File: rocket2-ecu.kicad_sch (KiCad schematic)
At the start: 25 parts, among them J1 ALARM, J2 SMA, P1 PAD_SMD, P2 PAD_SMD, P3 PAD_SMD, P4 PAD_SMD, Q1 DMG3402L

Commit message: ECU essentially reviewable
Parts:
- removed C2: 100nF, Capacitor_SMD:C_0603_1608Metric, symbol Device:C_Small
- removed C7: 10uF, Capacitor_SMD:C_0603_1608Metric, symbol Device:C_Small
- removed J2: SMA, Connector_Coaxial:SMA_Molex_73251-2200_Horizontal, symbol Connector:Conn_Coaxial
- removed U3: ~, Package_SO:SOIC-8W_5.3x5.3mm_P1.27mm, symbol UCIRP-KiCAD-Lib:SST25VF016B
- removed U4: ~, UCIRP-KiCAD-Lib:RFM95W, symbol UCIRP-KiCAD-Lib:RFM95W
- renumbered C3 to C2, C4 to C3, C5 to C4, C6 to C5, C8 to C6, U5 to U3, U6 to U4
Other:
- added sheet ECU_Memory (ECU_Memory.kicad_sch)
- added sheet ECU_Radios (ECU_Radios.kicad_sch)
- note added: "ECU Radios"
- note added: "I want this to actually work"
- note removed: "SOMETHING NEEDS TO BE FIXED IN EVE I FORGOT WHAT"
- note removed: "TRS Radio Module"

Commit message: addressed PR comments
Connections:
- no-connect marks 0 -> 1
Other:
- added sheet PT5 (pt.kicad_sch)
- added sheet PT6 (pt.kicad_sch)
- added sheet TC1 (tc.kicad_sch)
- note added: "1 extra TC (NEED TO ADD CS TO STM)"
- note added: "Two extra PTs for redundancy (5 and 6) (NEED TO ADD TO STM)"
- moved on the sheet: P1, P2, P3, P4

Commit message: Updated schematic with IOC
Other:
- note removed: "1 extra TC (NEED TO ADD CS TO STM)"
- note removed: "Two extra PTs for redundancy (5 and 6) (NEED TO ADD TO STM)"
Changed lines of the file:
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@@
-		)
-	)
-	(text "1 extra TC\n\n(NEED TO ADD CS \nTO STM)"
-		(exclude_from_sim no)
-		(at 113.284 174.244 0)
-		(effects
-			(font
-				(size 1.27 1.27)
-				(color 255 26 30 1)
-			)
-		)
-	)
-	(text "Two extra PTs \nfor redundancy \n(5 and 6)\n\n(NEED TO ADD TO STM)"
-		(exclude_from_sim no)
-		(at 69.85 148.844 0)
-		(effects
-			(font
-				(size 1.27 1.27)
-				(color 255 26 30 1)
-			)
 		)
 	)

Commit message: Assigned almost all footprints
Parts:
- C1, C2, C3, C4, C5: footprint Capacitor_SMD:C_0603_1608Metric -> Capacitor_SMD:C_0402_1005Metric; Part # (none) -> Generic 100nF 6.3V X7R 0402 MLCC
- P1, P2, P3, P4: footprint (none) -> TestPoint:TestPoint_Plated_Hole_D4.0mm
- R3, R4: footprint Resistor_SMD:R_0603_1608Metric -> Resistor_SMD:R_0402_1005Metric; Part # (none) -> Generic 4k7 1% 0402 Resistor
- U1: footprint UCIRP-KiCAD-Lib:BMI088 -> 0UCIRP-KiCAD-Lib:BMI088
- U2: footprint UCIRP-KiCAD-Lib:MS5607-02BA -> 0UCIRP-KiCAD-Lib:MS5607-02BA
- U4: footprint UCIRP-KiCAD-Lib:GC-XPORT -> 0UCIRP-KiCAD-Lib:GC-XPORT
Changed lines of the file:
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@@
 			)
 		)
-		(property "Footprint" "Resistor_SMD:R_0603_1608Metric"
+		(property "Footprint" "Resistor_SMD:R_0402_1005Metric"
 			(at 111.76 27.94 0)
 			(effects
@@
 			)
 		)
+		(property "Part #" "Generic 4k7 1% 0402 Resistor"
+			(at 111.76 27.94 0)
+			(effects
+				(font
+					(size 1.27 1.27)
+				)
+				(hide yes)
+			)
+		)
 		(pin "1"
 		)
@@
 			)
 		)
-		(property "Footprint" ""
+		(property "Footprint" "TestPoint:TestPoint_Plated_Hole_D4.0mm"
 			(at 30.48 27.94 0)
 			(effects
@@
 					(size 1.524 1.524)
 				)
+				(hide yes)
 			)
 		)
@@
 			)
 		)
-		(property "Footprint" "UCIRP-KiCAD-Lib:GC-XPORT"
+		(property "Footprint" "0UCIRP-KiCAD-Lib:GC-XPORT"
 			(at 256.54 153.67 0)
 			(effects
@@
 		(dnp no)
 		(fields_autoplaced yes)
-		(property "Reference" "#PWR01"
+		(property "Reference" "#PWR02"
 			(at 36.83 53.34 0)
 			(effects
@@
 			(project "rocket2-ecu"
 				(path "/02606b2c-b376-4ffb-9781-f9cea3f70994"
-					(reference "#PWR01")
+					(reference "#PWR02")
 					(unit 1)
 				)
@@
 			)
 		)
-		(property "Footprint" ""
+		(property "Footprint" "TestPoint:TestPoint_Plated_Hole_D4.0mm"
 			(at 30.48 24.13 0)
 			(effects
@@
 					(size 1.524 1.524)
 				)
+				(hide yes)
 			)
 		)
@@
 		(dnp no)
 		(fields_autoplaced yes)
-		(property "Reference" "#PWR02"
+		(property "Reference" "#PWR01"
 			(at 36.83 27.94 0)
 			(effects
@@
 			(project "rocket2-ecu"
 				(path "/02606b2c-b376-4ffb-9781-f9cea3f70994"
-					(reference "#PWR02")
+					(reference "#PWR01")
 					(unit 1)
 				)
@@
 			)
 		)
-		(property "Footprint" "UCIRP-KiCAD-Lib:MS5607-02BA"
+		(property "Footprint" "0UCIRP-KiCAD-Lib:MS5607-02BA"
 			(at 123.19 85.09 0)
 			(effects
@@
 			)
 		)
-		(property "Footprint" "Capacitor_SMD:C_0603_1608Metric"
+		(property "Footprint" "Capacitor_SMD:C_0402_1005Metric"
 			(at 154.94 134.62 0)
 			(effects
@@
 			)
 		)
+		(property "Part #" "Generic 100nF 6.3V X7R 0402 MLCC"
+			(at 154.94 134.62 0)
+			(effects
+				(font
+					(size 1.27 1.27)
+				)
+				(hide yes)
+			)
+		)
 		(pin "1"
 		)
@@
 			)
 		)
-		(property "Footprint" "Capacitor_SMD:C_0603_1608Metric"
+		(property "Footprint" "Capacitor_SMD:C_0402_1005Metric"
 			(at 151.13 24.13 0)
 			(effects
@@
 			)
 		)
+		(property "Part #" "Generic 100nF 6.3V X7R 0402 MLCC"
+			(at 151.13 24.13 0)
+			(effects
+				(font
+					(size 1.27 1.27)
+				)
+				(hide yes)
+			)
+		)
 		(pin "1"
 		)
@@
 			)
 		)
-		(property "Footprint" "Capacitor_SMD:C_0603_1608Metric"
+		(property "Footprint" "Capacitor_SMD:C_0402_1005Metric"
 			(at 88.9 83.82 0)
 			(effects
@@
 			)
 		)
+		(property "Part #" "Generic 100nF 6.3V X7R 0402 MLCC"
+			(at 88.9 83.82 0)
+			(effects
+				(font
+					(size 1.27 1.27)
+				)
+				(hide yes)
+			)
+		)
 		(pin "1"
 		)
@@
 			)
 		)
-		(property "Footprint" ""
+		(property "Footprint" "TestPoint:TestPoint_Plated_Hole_D4.0mm"
 			(at 30.48 15.24 0)
 			(effects
@@
 					(size 1.524 1.524)
 				)
+				(hide yes)
 			)
 		)
@@
 			)
 		)
-		(property "Footprint" "UCIRP-KiCAD-Lib:BMI088"
+		(property "Footprint" "0UCIRP-KiCAD-Lib:BMI088"
 			(at 113.03 134.62 0)
 			(effects
@@
 			)
 		)
-		(property "Footprint" "Capacitor_SMD:C_0603_1608Metric"
+		(property "Footprint" "Capacitor_SMD:C_0402_1005Metric"
 			(at 129.54 24.13 0)
 			(effects
@@
 			)
 		)
+		(property "Part #" "Generic 100nF 6.3V X7R 0402 MLCC"
+			(at 129.54 24.13 0)
+			(effects
+				(font
+					(size 1.27 1.27)
+				)
+				(hide yes)
+			)
+		)
 		(pin "1"
 		)
@@
 			)
 		)
-		(property "Footprint" "Resistor_SMD:R_0603_1608Metric"
+		(property "Footprint" "Resistor_SMD:R_0402_1005Metric"
 			(at 115.57 41.91 0)
 			(effects
@@
 			)
 		)
+		(property "Part #" "Generic 4k7 1% 0402 Resistor"
+			(at 115.57 41.91 0)
+			(effects
+				(font
+					(size 1.27 1.27)
+				)
+				(hide yes)
+			)
+		)
 		(pin "1"
 		)
@@
 			)
 		)
-		(property "Footprint" "Capacitor_SMD:C_0603_1608Metric"
+		(property "Footprint" "Capacitor_SMD:C_0402_1005Metric"
 			(at 143.51 134.62 0)
 			(effects
@@
 			)
 		)
+		(property "Part #" "Generic 100nF 6.3V X7R 0402 MLCC"
+			(at 143.51 134.62 0)
+			(effects
+				(font
+					(size 1.27 1.27)
+				)
+				(hide yes)
+			)
+		)
 		(pin "1"
 		)
@@
 			)
 		)
-		(property "Footprint" ""
+		(property "Footprint" "TestPoint:TestPoint_Plated_Hole_D4.0mm"
 			(at 30.48 19.05 0)
 			(effects
@@
 					(size 1.524 1.524)
 				)
+				(hide yes)
 			)
 		)

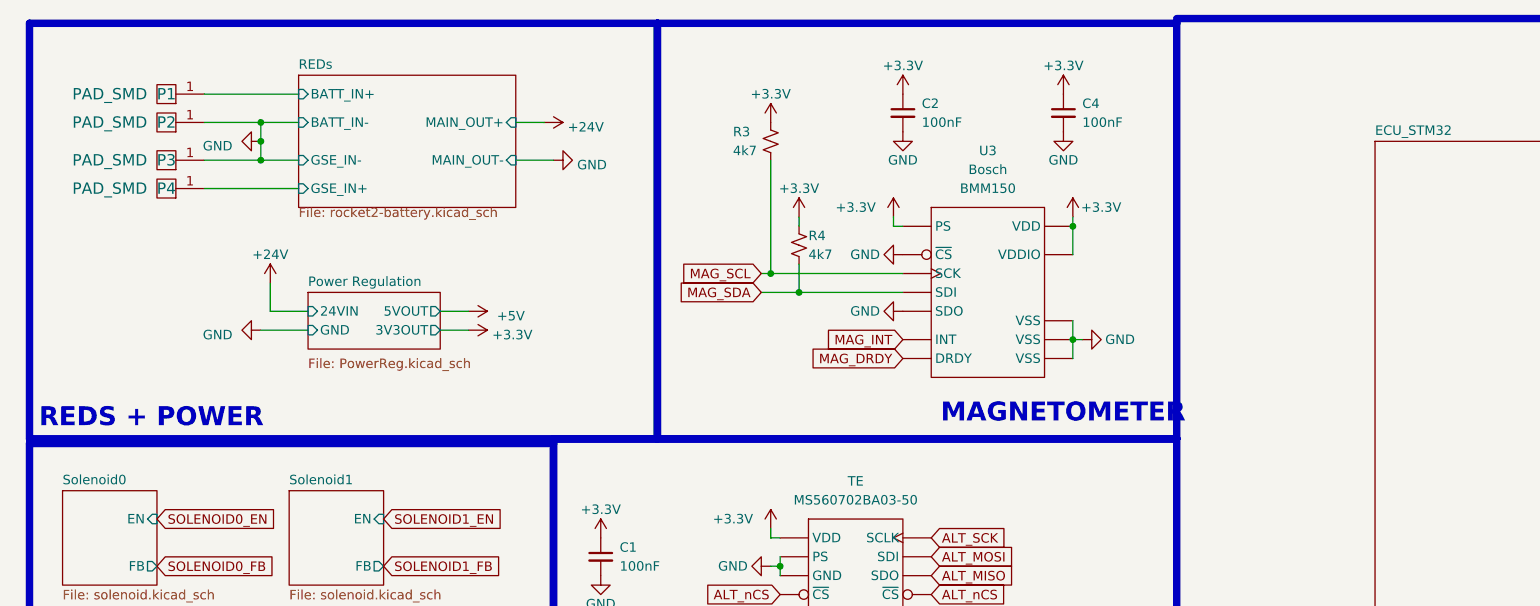
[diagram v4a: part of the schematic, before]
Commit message: Added mounting holes
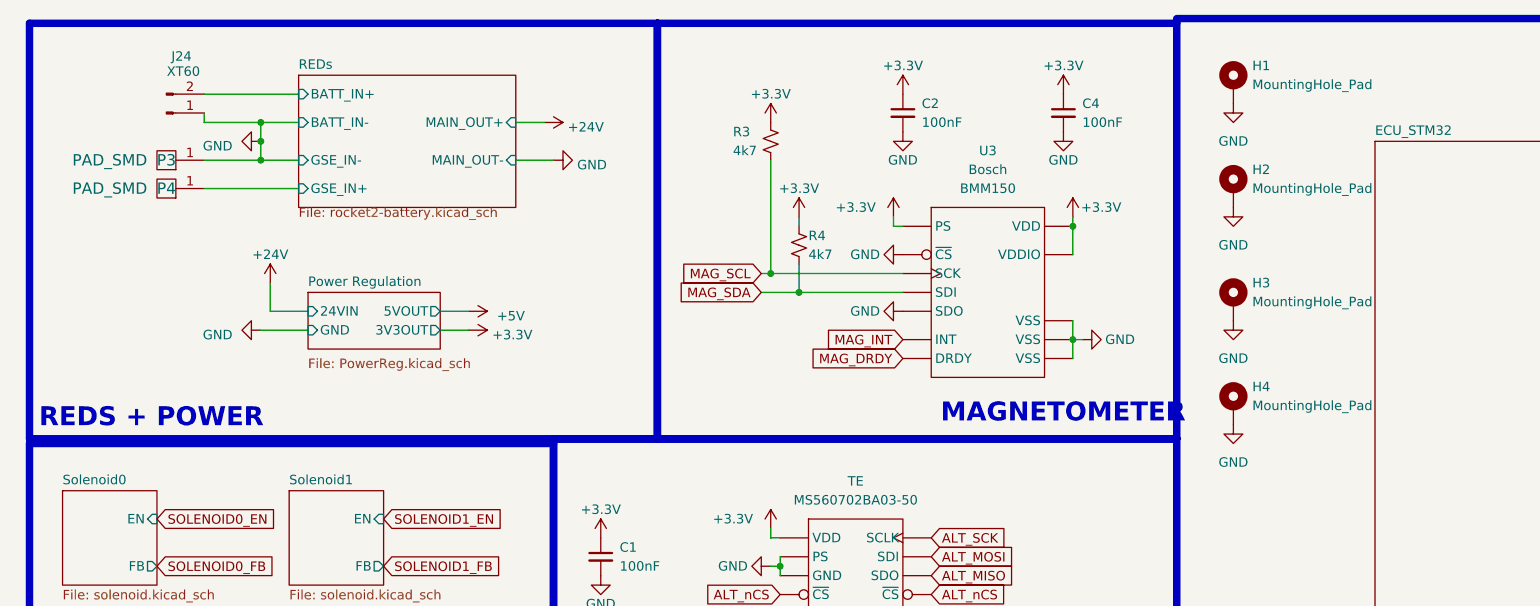
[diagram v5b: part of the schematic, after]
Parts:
- removed P1, P2: PAD_SMD, TestPoint:TestPoint_Plated_Hole_D4.0mm, symbol pkl_misc:PAD_SMD
- added H1, H2, H3, H4: MountingHole_Pad, MountingHole:MountingHole_4.3mm_M4_Pad_Via, symbol Mechanical:MountingHole_Pad
- added J24: XT60, Connector_AMASS:AMASS_XT60PW-M_1x02_P7.20mm_Horizontal, symbol Connector:Conn_01x02_Pin
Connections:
- net GND: now also H1.1, H2.1, H3.1, H4.1, J24.1 (Pin_1)
- net REDs/BATT_IN+: now also J24.2 (Pin_2)

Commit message: Updated with Daniels suggestions
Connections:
- no-connect marks 1 -> 3
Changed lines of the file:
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@@
+	)
+	(no_connect
+		(at 194.31 148.59)
+	)
+	(no_connect
+		(at 194.31 144.78)
 	)
 	(no_connect
@@
 		)
 	)
-	(global_label "GPS_SDA"
-		(shape input)
-		(at 194.31 144.78 180)
+	(global_label "MAG_SCL"
+		(shape input)
+		(at 110.49 45.72 180)
 		(fields_autoplaced yes)
 		(effects
@@
 		)
 		(property "Intersheetrefs" "${INTERSHEET_REFS}"
-			(at 183.0396 144.78 0)
+			(at 99.2196 45.72 0)
 			(effects
 				(font
@@
 		)
 	)
-	(global_label "MAG_SCL"
-		(shape input)
-		(at 110.49 45.72 180)
-		(fields_autoplaced yes)
-		(effects
-			(font
-				(size 1.27 1.27)
-			)
-			(justify right)
-		)
-		(property "Intersheetrefs" "${INTERSHEET_REFS}"
-			(at 99.2196 45.72 0)
-			(effects
-				(font
-					(size 1.27 1.27)
-				)
-				(justify right)
-				(hide yes)
-			)
-		)
-	)
 	(global_label "SOLENOID2_EN"
 		(shape input)
@@
 				(hide yes)
 			)
-		)
-	)
-	(global_label "GPS_SCL"
-		(shape input)
-		(at 194.31 148.59 180)
-		(fields_autoplaced yes)
-		(effects
-			(font
-				(size 1.27 1.27)
-			)
-			(justify right)
-		)
-		(property "Intersheetrefs" "${INTERSHEET_REFS}"
-			(at 183.1001 148.59 0)
-			(effects
-				(font
-					(size 1.27 1.27)
-				)
-				(justify right)
-				(hide yes)
-			)

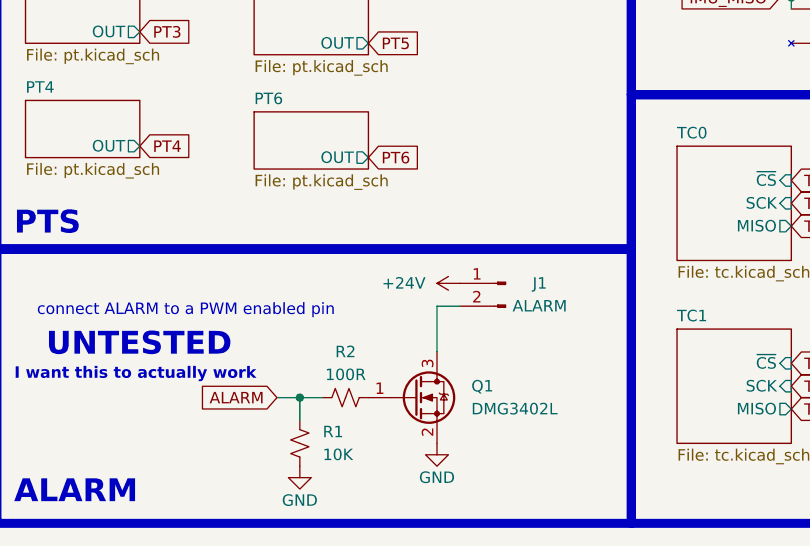
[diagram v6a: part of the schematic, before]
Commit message: Added buzzer
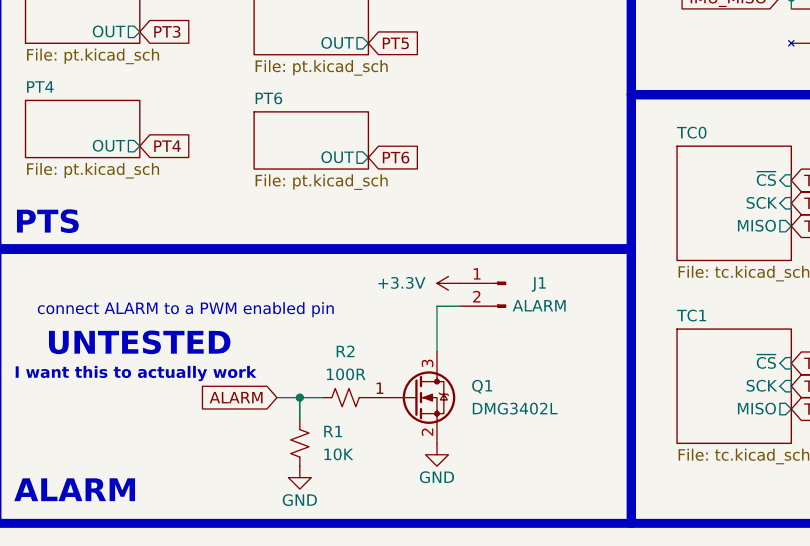
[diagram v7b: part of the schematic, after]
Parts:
- J1: footprint TerminalBlock:TerminalBlock_bornier-2_P5.08mm -> 0UCIRP-KiCAD-Lib:CMI-0955-03TH_Buzzer; Manufacturer (none) -> Same Sky; Part # (none) -> CMI-0955-03TH
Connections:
- net +24V: no longer J1.1 (Pin_1)
- net +3.3V: now also J1.1 (Pin_1)
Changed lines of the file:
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@@
 	)
 	(symbol
-		(lib_id "power:+24V")
-		(at 63.5 171.45 90)
-		(mirror x)
-		(unit 1)
-		(exclude_from_sim no)
-		(in_bom yes)
-		(on_board yes)
-		(dnp no)
-		(property "Reference" "#PWR06"
-			(at 67.31 171.45 0)
-			(effects
-				(font
-					(size 1.27 1.27)
-				)
-				(hide yes)
-			)
-		)
-		(property "Value" "+24V"
-			(at 59.69 171.45 90)
-			(effects
-				(font
-					(size 1.27 1.27)
-				)
-				(justify left)
-			)
-		)
-		(property "Footprint" ""
-			(at 63.5 171.45 0)
-			(effects
-				(font
-					(size 1.27 1.27)
-				)
-				(hide yes)
-			)
-		)
-		(property "Datasheet" ""
-			(at 63.5 171.45 0)
-			(effects
-				(font
-					(size 1.27 1.27)
-				)
-				(hide yes)
-			)
-		)
-		(property "Description" ""
-			(at 63.5 171.45 0)
-			(effects
-				(font
-					(size 1.27 1.27)
-				)
-				(hide yes)
-			)
-		)
-		(pin "1"
-		)
-		(instances
-			(project "rocket2-ecu"
-				(path "/02606b2c-b376-4ffb-9781-f9cea3f70994"
-					(reference "#PWR06")
-					(unit 1)
-				)
-			)
-			(project "rocket2-gse"
-				(path "/94c3ca0c-6aa1-4bff-ab47-a0279d059895"
-					(reference "#PWR058")
-					(unit 1)
-				)
-			)
-		)
-	)
-	(symbol
 		(lib_id "UCIRP-KiCAD-Lib:GC-XPORT")
 		(at 256.54 153.67 0)
@@
 	)
 	(symbol
+		(lib_name "+3.3V_1")
+		(lib_id "power:+3.3V")
+		(at 63.5 171.45 90)
+		(unit 1)
+		(exclude_from_sim no)
+		(in_bom yes)
+		(on_board yes)
+		(dnp no)
+		(fields_autoplaced yes)
+		(property "Reference" "#PWR06"
+			(at 67.31 171.45 0)
+			(effects
+				(font
+					(size 1.27 1.27)
+				)
+				(hide yes)
+			)
+		)
+		(property "Value" "+3.3V"
+			(at 59.69 171.4499 90)
+			(effects
+				(font
+					(size 1.27 1.27)
+				)
+				(justify left)
+			)
+		)
+		(property "Footprint" ""
+			(at 63.5 171.45 0)
+			(effects
+				(font
+					(size 1.27 1.27)
+				)
+				(hide yes)
+			)
+		)
+		(property "Datasheet" ""
+			(at 63.5 171.45 0)
+			(effects
+				(font
+					(size 1.27 1.27)
+				)
+				(hide yes)
+			)
+		)
+		(property "Description" "Power symbol creates a global label with name \"+3.3V\""
+			(at 63.5 171.45 0)
+			(effects
+				(font
+					(size 1.27 1.27)
+				)
+				(hide yes)
+			)
+		)
+		(pin "1"
+		)
+		(instances
+			(project "rocket2-ecu"
+				(path "/02606b2c-b376-4ffb-9781-f9cea3f70994"
+					(reference "#PWR06")
+					(unit 1)
+				)
+			)
+		)
+	)
+	(symbol
 		(lib_name "GND_1")
 		(lib_id "power:GND")
@@
 			)
 		)
-		(property "Footprint" "TerminalBlock:TerminalBlock_bornier-2_P5.08mm"
+		(property "Footprint" "0UCIRP-KiCAD-Lib:CMI-0955-03TH_Buzzer"
 			(at 68.58 171.45 0)
 			(effects
@@
 			)
 		)
-		(property "Datasheet" "~"
+		(property "Datasheet" "https://www.mouser.com/datasheet/2/1628/cmi_0955_03th-3513045.pdf"
 			(at 68.58 171.45 0)
 			(effects
@@
 			)
 		)
-		(property "Description" "https://www.mouser.com/datasheet/2/1005/202104270e382-2325619.pdf Maybe?"
+		(property "Description" "~"
 			(at 68.58 171.45 0)
 			(effects
@@
 			)
 		)
-		(property "Manufacturer" "~"
+		(property "Manufacturer" "Same Sky"
 			(at 68.58 171.45 0)
 			(effects
@@
 			)
 		)
-		(property "Part #" "~"
+		(property "Part #" "CMI-0955-03TH "
 			(at 68.58 171.45 0)
 			(effects

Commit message: notes
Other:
- note added: "FIC GROUND VIAS AND RETURN PATHS"
- note added: "Reads battery voltage Reads GSE voltage"
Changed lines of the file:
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@@
+		)
+	)
+	(text "FIC GROUND VIAS AND RETURN PATHS"
+		(exclude_from_sim no)
+		(at 66.548 61.976 0)
+		(effects
+			(font
+				(size 1.27 1.27)
+				(color 255 41 27 1)
+			)
 		)
 	)
@@
 		)
 	)
+	(text "Reads battery voltage\nReads GSE voltage"
+		(exclude_from_sim no)
+		(at 251.968 125.222 0)
+		(effects
+			(font
+				(size 1.27 1.27)
+				(color 255 41 27 1)
+			)
+		)
+	)
